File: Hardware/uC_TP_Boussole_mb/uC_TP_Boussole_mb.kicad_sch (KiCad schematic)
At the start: 0 parts

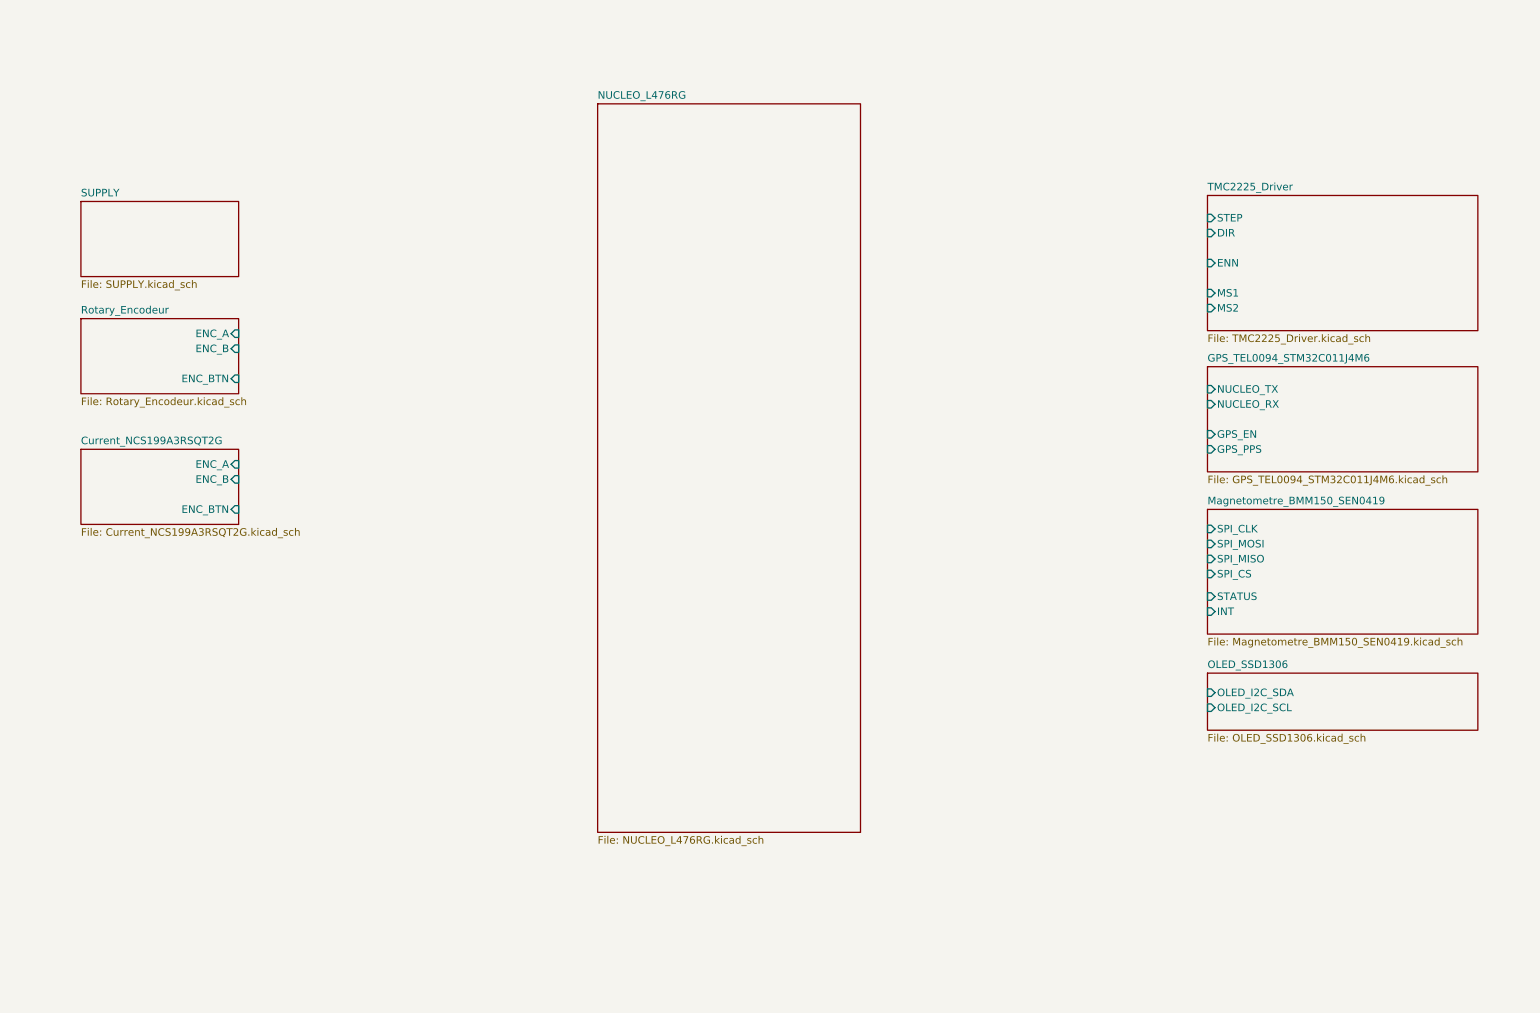
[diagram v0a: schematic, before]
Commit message: starting pin out nucleo
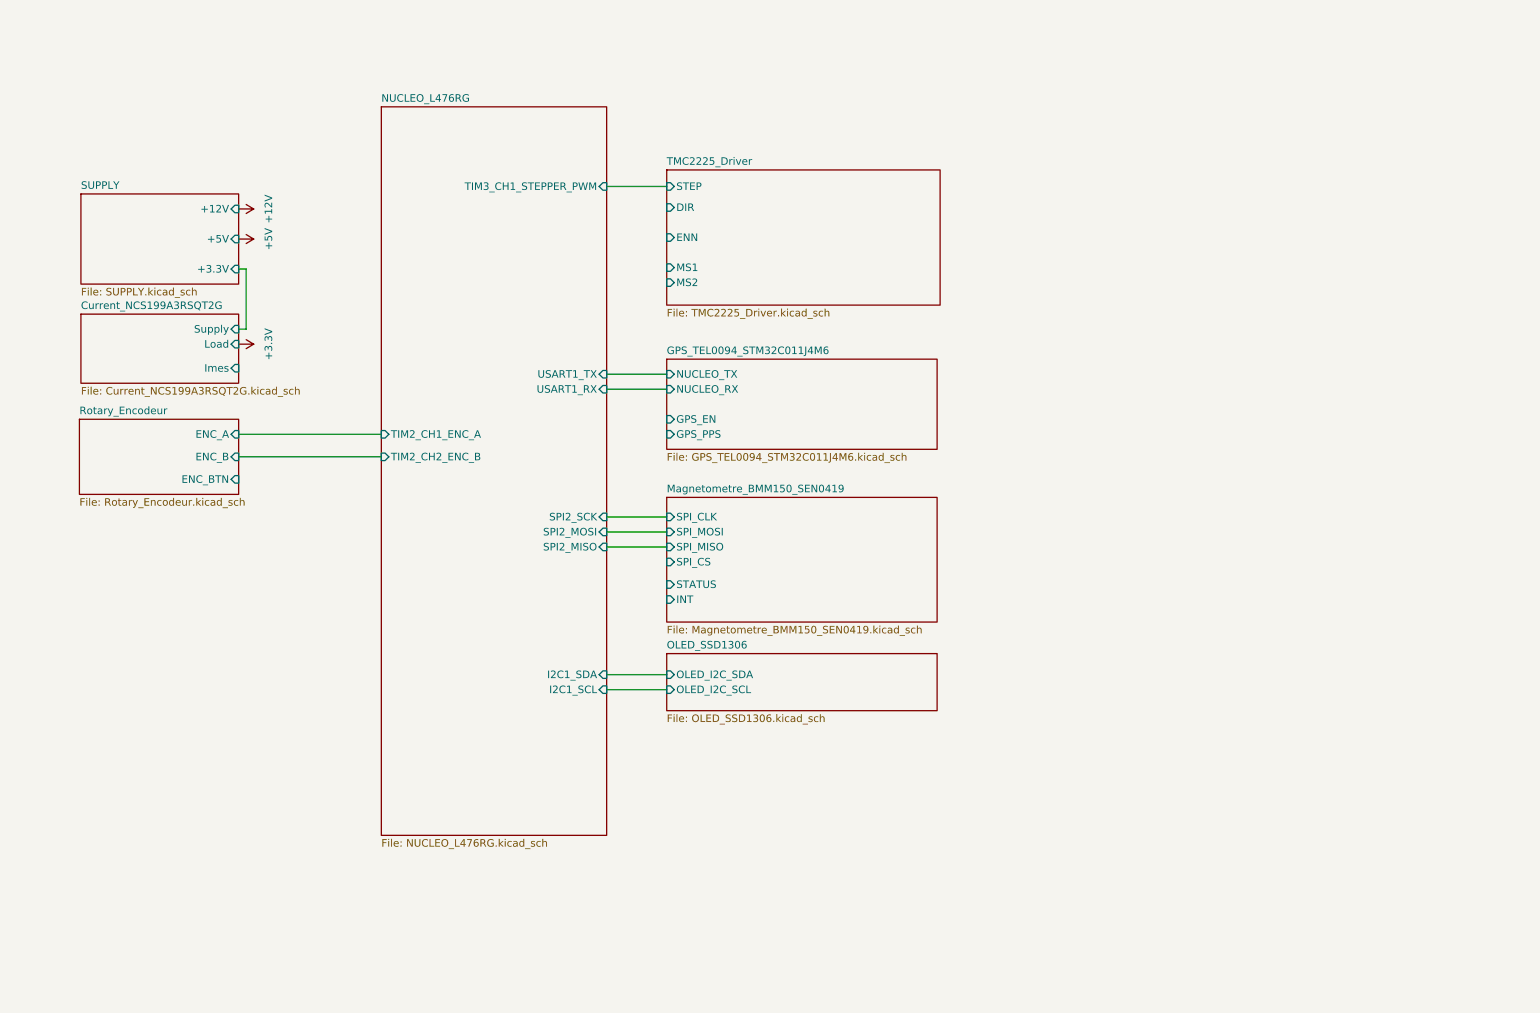
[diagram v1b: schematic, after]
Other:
- sheet Current_NCS199A3RSQT2G ports: added Imes, Load, Supply; removed ENC_A, ENC_B, ENC_BTN
- sheet NUCLEO_L476RG ports: added I2C1_SCL, I2C1_SDA, SPI2_MISO, SPI2_MOSI, SPI2_SCK, TIM2_CH1_ENC_A, TIM2_CH2_ENC_B, TIM3_CH1_STEPPER_PWM, USART1_RX, USART1_TX; removed none
- sheet SUPPLY ports: added +12V, +3.3V, +5V; removed none

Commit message: update pcb
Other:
- note added: "A faire, Mesure courant sur le 5V de la Nucleo Rajouter 8 leds + bouton Led RGB sur 3 canaux d'une PWM Augmenter Rsense pour limiter le courant"
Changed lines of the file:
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@@
+		)
+	)
+	(text "A faire,\nMesure courant sur le 5V de la Nucleo\nRajouter 8 leds + bouton\nLed RGB sur 3 canaux d'une PWM\nAugmenter Rsense pour limiter le courant\n"
+		(exclude_from_sim no)
+		(at 13.716 18.034 0)
+		(effects
+			(font
+				(size 1.27 1.27)
+			)
+			(justify left)
 		)
 	)

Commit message: update ppcb
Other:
- sheet NUCLEO_L476RG ports: added E5V, ENC_BTN, GPS_EN, GPS_PPS, MAGNETO_INT, MAGNETO_STATUS, SPI_CS, STEPPER_DIR, STEPPER_ENN, STEPPER_MS1, STEPPER_MS2, V_Imes; removed none

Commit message: finalize pcb
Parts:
- added H101, H102, H103, H104, H105, H106, H107, H108: MountingHole_Pad, MountingHole:MountingHole_3.2mm_M3_Pad, symbol Mechanical:MountingHole_Pad
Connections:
- new net GND: H101.1, H102.1, H103.1, H104.1, H105.1, H106.1, H107.1, H108.1
